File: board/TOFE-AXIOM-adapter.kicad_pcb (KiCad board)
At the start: 2 copper layers, 68.9 x 28.3 mm, 3 parts, among them U1 TOFE_8X_HL_NW, U2 TOFE_8X_HL_NW

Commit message: Slowly working on the adapter.
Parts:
- removed U2: TOFE_8X_HL_NW, PCIe_98Pos

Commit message: Starting work on the PCB.
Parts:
- U1: value TOFE_8X_HL_NW -> TOFE-8X
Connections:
- net /A13 renamed /N_IO0
- net /A14 renamed /S_IO0
- net /A16 renamed /S_LVDS_A0
- net /A17 renamed /S_LVDS_B0
- net /A19 renamed /S_IO4
- net /A21 renamed /S_LVDS_A1
- net /A22 renamed /S_LVDS_B1
- net /A25 renamed /S_LVDS_A2
- net /A26 renamed /S_LVDS_B2
- net /A29 renamed /S_LVDS_A3
- net /A30 renamed /S_LVDS_B3
- net /A32 renamed /S_IO3
- net /A33 renamed Net-(U1-PadA33)
- net /A35 renamed /S_LVDS_A4
- net /A36 renamed /S_LVDS_B4
- net /A39 renamed /S_LVDS_A5
- net /A40 renamed /S_LVDS_B5
- net /A43 renamed /S_IO2
- net /A44 renamed /S_IO1
- net /A47 renamed /S_SDA
- net /A48 renamed /S_SCL
- net /A5 renamed /S_IO7
- net /A6 renamed /S_IO6
- net /A7 renamed /N_IO7
- net /A8 renamed /N_IO6
- net /B14 renamed /N_LVDS_A0
- net /B15 renamed /N_LVDS_B0
- net /B19 renamed /N_LVDS_A1
- net /B20 renamed /N_LVDS_B1
- net /B23 renamed /N_LVDS_A2
- net /B24 renamed /N_LVDS_B2
- net /B27 renamed /N_LVDS_A3
- net /B28 renamed /N_LVDS_B3
- net /B30 renamed /N_IO3
- net /B33 renamed /N_LVDS_A4
- net /B34 renamed /N_LVDS_B4
- net /B37 renamed /N_LVDS_A5
- net /B38 renamed /N_LVDS_B5
- net /B41 renamed /N_IO2
- net /B42 renamed /N_IO1
- net /B45 renamed /N_SDA
- net /B46 renamed /N_SCL
- net /B5 renamed /SMCLK
- net /B6 renamed /SMDAT
- net /B9 renamed /S_IO5
- net /GND renamed GND
- U1 pad B11: /B11 -> /N_IO4
- U1 pad B12: /B12 -> /N_IO4
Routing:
- net (no net): track 0.00 -> 113.2 mm, vias 0 -> 20
- net GND: track 284.7 -> 189.4 mm, vias 42 -> 24
- net /N_IO4: track 0.00 -> 51.2 mm
- net /B11: track 25.6 -> 0.00 mm
- net /B12: track 25.6 -> 0.00 mm
- net /S_LVDS_A4: track 25.4 -> 11.1 mm
- net /VCC3V3: track 39.5 -> 36.0 mm, vias 6 -> 4
- added copper zone on B.Cu, net /GND
- added copper zone on F.Cu, net /GND
- removed copper zone on B.Cu, net GND
- removed copper zone on F.Cu, net GND

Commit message: Slowly getting there.
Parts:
- added JP***: pci-x_conn-x1, w_conn_pc:pci-x_conn-x1, F.Cu at (184.0, 167.1)
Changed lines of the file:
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@@
 (kicad_pcb (version 4) (host pcbnew 4.0.2-4+6225~38~ubuntu14.04.1-stable)
   (general
-    (links 141)
+    (links 0)
     (no_connects 39)
-    (area 162.059499 159.613599 231.355901 188.340501)
+    (area 128.5788 159.613599 231.355901 189.2154)
     (thickness 1.6)
     (drawings 20)
     (tracks 1286)
     (zones 0)
-    (modules 2)
+    (modules 3)
     (nets 53)
   )
@@
       (xy 2.794 2.62382)) (layer F.SilkS) (width 0.00254))
   )
+  (module w_conn_pc:pci-x_conn-x1 (layer F.Cu)
+    (at 183.9976 167.0812)
+    (descr "PCI-X 1x card edge connector, FCI P/N 10018783-10x00x")
+    (fp_text reference JP*** (at 0 -5.99948) (layer F.SilkS)
+      (effects (font (thickness 0.3048)))
+    )
+    (fp_text value pci-x_conn-x1 (at 0 7.00024) (layer F.SilkS)
+      (effects (font (thickness 0.3048)))
+    )
+    (fp_line (start 1.09982 -0.89916) (end -10.59942 -0.89916) (layer F.SilkS) (width 0.3048))
+    (fp_line (start -10.59942 -0.89916) (end -10.59942 0.89916) (layer F.SilkS) (width 0.3048))
+    (fp_line (start 1.09982 0.89916) (end -10.59942 0.89916) (layer F.SilkS) (width 0.3048))
+    (fp_line (start 2.90068 0.89916) (end 2.90068 -0.89916) (layer F.SilkS) (width 0.3048))
+    (fp_line (start 2.90068 -0.89916) (end 10.55116 -0.89916) (layer F.SilkS) (width 0.3048))
+    (fp_line (start 10.55116 -0.89916) (end 10.55116 0.89916) (layer F.SilkS) (width 0.3048))
+    (fp_line (start 10.55116 0.89916) (end 2.90068 0.89916) (layer F.SilkS) (width 0.3048))
+    (fp_line (start 1.09982 0.89916) (end 1.09982 -0.89916) (layer F.SilkS) (width 0.3048))
+    (fp_line (start 9.10082 3.70078) (end 9.10082 5.19938) (layer F.SilkS) (width 0.3048))
+    (fp_line (start 9.10082 5.19938) (end 12.49934 5.19938) (layer F.SilkS) (width 0.3048))
+    (fp_line (start 12.49934 5.19938) (end 12.49934 3.70078) (layer F.SilkS) (width 0.3048))
+    (fp_line (start 0.8001 3.70078) (end 0.8001 5.19938) (layer F.SilkS) (width 0.3048))
+    (fp_line (start 0.8001 5.19938) (end 7.59968 5.19938) (layer F.SilkS) (width 0.3048))
+    (fp_line (start 7.59968 5.19938) (end 7.59968 3.70078) (layer F.SilkS) (width 0.3048))
+    (fp_line (start -7.59968 5.19938) (end -0.8001 5.19938) (layer F.SilkS) (width 0.3048))
+    (fp_line (start -0.8001 5.19938) (end -0.8001 3.70078) (layer F.SilkS) (width 0.3048))
+    (fp_line (start -7.59968 3.70078) (end -7.59968 5.19938) (layer F.SilkS) (width 0.3048))
+    (fp_line (start -12.49934 3.70078) (end -12.49934 5.19938) (layer F.SilkS) (width 0.3048))
+    (fp_line (start -12.49934 5.19938) (end -9.10082 5.19938) (layer F.SilkS) (width 0.3048))
+    (fp_line (start -9.10082 5.19938) (end -9.10082 3.70078) (layer F.SilkS) (width 0.3048))
+    (fp_line (start -12.49934 -3.70078) (end -12.49934 3.70078) (layer F.SilkS) (width 0.3048))
+    (fp_line (start -12.49934 3.70078) (end 12.49934 3.70078) (layer F.SilkS) (width 0.3048))
+    (fp_line (start 12.49934 3.70078) (end 12.49934 -3.70078) (layer F.SilkS) (width 0.3048))
+    (fp_line (start 12.49934 -3.70078) (end -12.49934 -3.70078) (layer F.SilkS) (width 0.3048))
+    (pad "" np_thru_hole circle (at 2.14884 0) (size 2.4003 2.4003) (drill 2.4003) (layers *.Cu F.SilkS))
+    (pad "" np_thru_hole circle (at 11.30046 0) (size 2.4003 2.4003) (drill 2.4003) (layers *.Cu F.SilkS))
+    (pad A12 thru_hole circle (at 3.50012 -3.2512) (size 1.19888 1.19888) (drill 0.8001) (layers *.Cu *.Mask))
+    (pad A13 thru_hole circle (at 4.50088 -1.24968) (size 1.19888 1.19888) (drill 0.8001) (layers *.Cu *.Mask))
+    (pad A14 thru_hole circle (at 5.4991 -3.2512) (size 1.19888 1.19888) (drill 0.8001) (layers *.Cu *.Mask))
+    (pad A15 thru_hole circle (at 6.49986 -1.24968) (size 1.19888 1.19888) (drill 0.8001) (layers *.Cu *.Mask))
+    (pad A16 thru_hole circle (at 7.50062 -3.2512) (size 1.19888 1.19888) (drill 0.8001) (layers *.Cu *.Mask))
+    (pad A17 thru_hole circle (at 8.49884 -1.24968) (size 1.19888 1.19888) (drill 0.8001) (layers *.Cu *.Mask))
+    (pad A18 thru_hole circle (at 9.4996 -3.2512) (size 1.19888 1.19888) (drill 0.8001) (layers *.Cu *.Mask))
+    (pad B13 thru_hole circle (at 4.50088 1.24968) (size 1.19888 1.19888) (drill 0.8001) (layers *.Cu *.Mask))
+    (pad B15 thru_hole circle (at 6.49986 1.24968) (size 1.19888 1.19888) (drill 0.8001) (layers *.Cu *.Mask))
+    (pad B17 thru_hole circle (at 8.49884 1.24968) (size 1.19888 1.19888) (drill 0.8001) (layers *.Cu *.Mask))
+    (pad B12 thru_hole circle (at 3.50012 3.2512) (size 1.19888 1.19888) (drill 0.8001) (layers *.Cu *.Mask))
+    (pad B14 thru_hole circle (at 5.4991 3.2512) (size 1.19888 1.19888) (drill 0.8001) (layers *.Cu *.Mask))
+    (pad B16 thru_hole circle (at 7.50062 3.2512) (size 1.19888 1.19888) (drill 0.8001) (layers *.Cu *.Mask))
+    (pad B18 thru_hole circle (at 9.4996 3.2512) (size 1.19888 1.19888) (drill 0.8001) (layers *.Cu *.Mask))
+    (pad A11 thru_hole circle (at 0.50038 -1.24968) (size 1.19888 1.19888) (drill 0.8001) (layers *.Cu *.Mask))
+    (pad A9 thru_hole circle (at -1.50114 -1.24968) (size 1.19888 1.19888) (drill 0.8001) (layers *.Cu *.Mask))
+    (pad A7 thru_hole circle (at -3.50012 -1.24968) (size 1.19888 1.19888) (drill 0.8001) (layers *.Cu *.Mask))
+    (pad A5 thru_hole circle (at -5.4991 -1.24968) (size 1.19888 1.19888) (drill 0.8001) (layers *.Cu *.Mask))
+    (pad A3 thru_hole circle (at -7.50062 -1.24968) (size 1.19888 1.19888) (drill 0.8001) (layers *.Cu *.Mask))
+    (pad A1 thru_hole circle (at -9.4996 -1.24968) (size 1.19888 1.19888) (drill 0.8001) (layers *.Cu *.Mask))
+    (pad A2 thru_hole circle (at -8.49884 -3.2512) (size 1.19888 1.19888) (drill 0.8001) (layers *.Cu *.Mask))
+    (pad A4 thru_hole circle (at -6.49986 -3.2512) (size 1.19888 1.19888) (drill 0.8001) (layers *.Cu *.Mask))
+    (pad A6 thru_hole circle (at -4.50088 -3.2512) (size 1.19888 1.19888) (drill 0.8001) (layers *.Cu *.Mask))
+    (pad A8 thru_hole circle (at -2.49936 -3.2512) (size 1.19888 1.19888) (drill 0.8001) (layers *.Cu *.Mask))
+    (pad A10 thru_hole circle (at -0.50038 -3.2512) (size 1.19888 1.19888) (drill 0.8001) (layers *.Cu *.Mask))
+    (pad B1 thru_hole circle (at -9.4996 1.24968) (size 1.19888 1.19888) (drill 0.8001) (layers *.Cu *.Mask))
+    (pad B2 thru_hole circle (at -8.49884 3.2512) (size 1.19888 1.19888) (drill 0.8001) (layers *.Cu *.Mask))
+    (pad B3 thru_hole circle (at -7.50062 1.24968) (size 1.19888 1.19888) (drill 0.8001) (layers *.Cu *.Mask))
+    (pad B4 thru_hole circle (at -6.49986 3.2512) (size 1.19888 1.19888) (drill 0.8001) (layers *.Cu *.Mask))
+    (pad B5 thru_hole circle (at -5.4991 1.24968) (size 1.19888 1.19888) (drill 0.8001) (layers *.Cu *.Mask))
+    (pad B6 thru_hole circle (at -4.50088 3.2512) (size 1.19888 1.19888) (drill 0.8001) (layers *.Cu *.Mask))
+    (pad B7 thru_hole circle (at -3.50012 1.24968) (size 1.19888 1.19888) (drill 0.8001) (layers *.Cu *.Mask))
+    (pad B8 thru_hole circle (at -2.49936 3.2512) (size 1.19888 1.19888) (drill 0.8001) (layers *.Cu *.Mask))
+    (pad B9 thru_hole circle (at -1.50114 1.24968) (size 1.19888 1.19888) (drill 0.8001) (layers *.Cu *.Mask))
+    (pad B10 thru_hole circle (at -0.50038 3.2512) (size 1.19888 1.19888) (drill 0.8001) (layers *.Cu *.Mask))
+    (pad B11 thru_hole circle (at 0.50038 1.24968) (size 1.19888 1.19888) (drill 0.8001) (layers *.Cu *.Mask))
+    (model walter/conn_pc/pci-x_conn-x1.wrl
+      (at (xyz 0 0 0))
+      (scale (xyz 1 1 1))
+      (rotate (xyz 0 0 0))
+    )
+  )
   (gr_line (start 174 175.67736) (end 173.75 175.42736) (angle 90) (layer Edge.Cuts) (width 0.381))

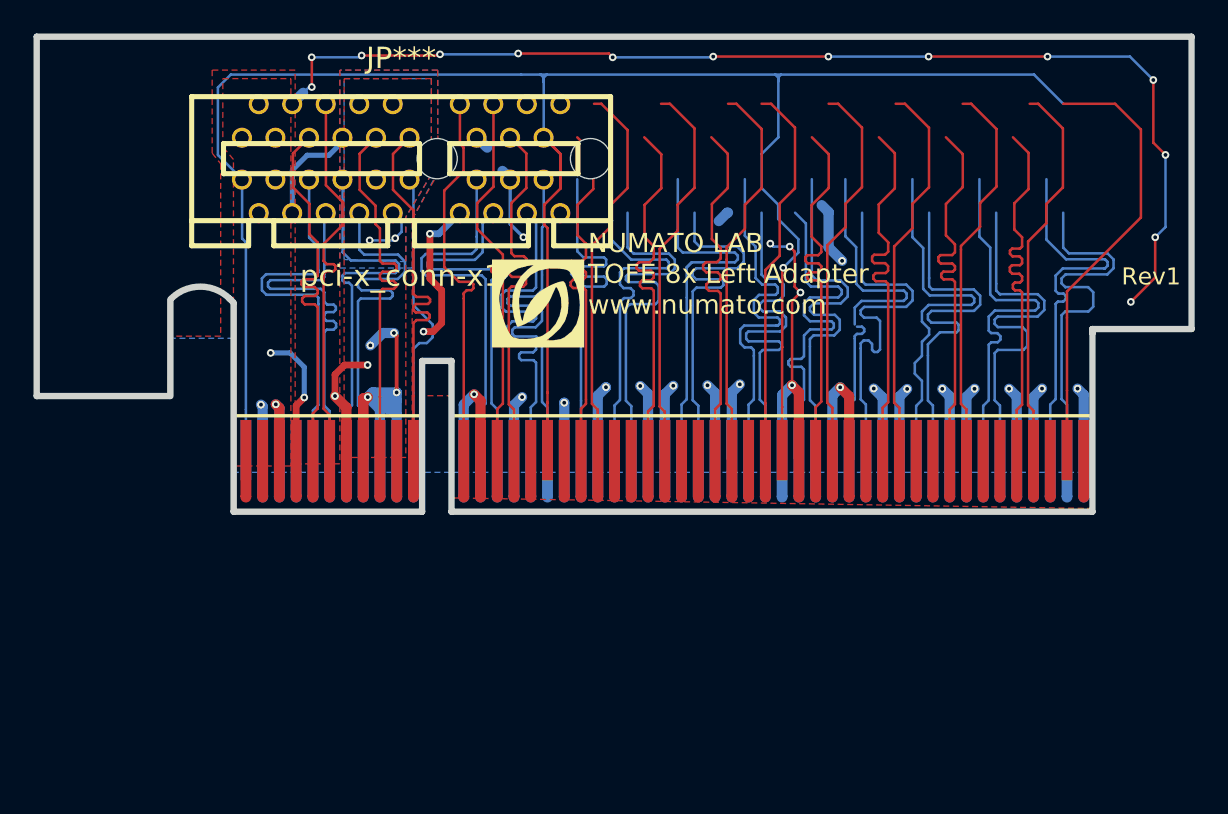
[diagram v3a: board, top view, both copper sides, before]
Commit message: Remove most of the routing from the PCB.
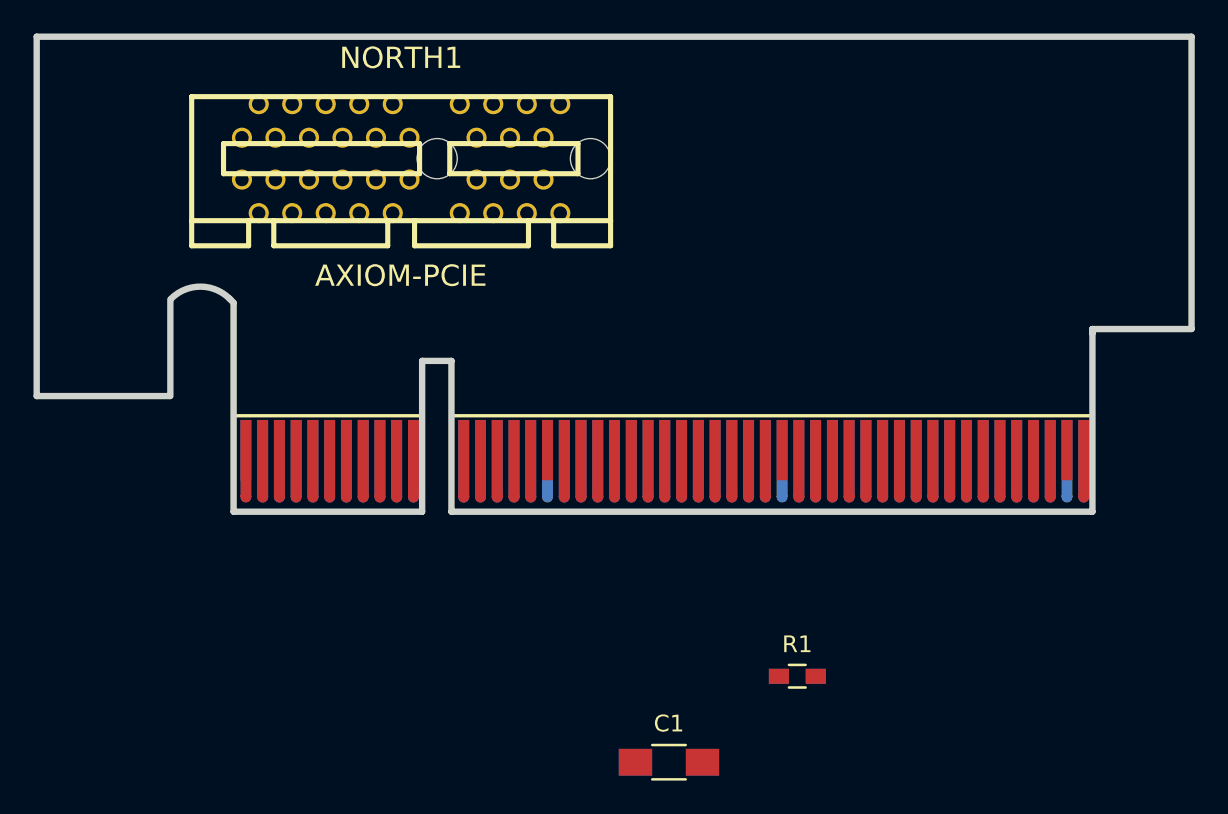
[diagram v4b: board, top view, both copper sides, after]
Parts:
- removed G***: LOGO, LOGO
- removed JP***: pci-x_conn-x1, w_conn_pc:pci-x_conn-x1
- added C1: C, Capacitors_SMD:C_1206_HandSoldering, F.Cu at (200.0, 203.1)
- added NORTH1: AXIOM-PCIE, w_conn_pc:pci-x_conn-x1, F.Cu at (184.0, 167.1)
- added R1: R, Resistors_SMD:R_0603_HandSoldering, F.Cu at (207.6, 198.0)
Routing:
- net GND: track 189.4 -> 13.8 mm, vias 24 -> 0
- net /PRSTN: track 152.1 -> 0.00 mm, vias 1 -> 0
- net (no net): track 113.2 -> 0.00 mm, vias 20 -> 0
- net /N_IO4: track 51.2 -> 2.30 mm
- net /VCC3V3: track 36.0 -> 0.00 mm, vias 4 -> 0
- net /S_IO3: track 25.6 -> 0.00 mm
- net Net-(U1-PadA33): track 25.6 -> 0.00 mm
- net /S_LVDS_A1: track 25.6 -> 0.00 mm
- net /SMCLK: track 25.6 -> 0.00 mm
- net /N_LVDS_A1: track 25.6 -> 0.00 mm
- net /N_LVDS_A0: track 25.6 -> 0.00 mm
- net /S_LVDS_B0: track 25.6 -> 0.00 mm
- net /S_SCL: track 25.6 -> 0.00 mm
- net /S_IO7: track 25.6 -> 0.00 mm
- net /N_LVDS_B0: track 25.6 -> 0.00 mm
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- removed copper zone on B.Cu, net /GND
- removed copper zone on F.Cu, net /GND
- removed copper zone on F.Cu, net /VCC12V
- removed copper zone on B.Cu, net /VCC3V3
- removed copper zone on F.Cu, net /VCC3V3
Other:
- board text removed: "NUMATO LAB TOFE 8x Left Adapter www.numato.com"
- board text removed: "Rev1"
